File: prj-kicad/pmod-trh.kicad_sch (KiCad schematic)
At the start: 14 parts, among them P1 PMOD, U1 ATSAMD09C13A, U2 SI7021

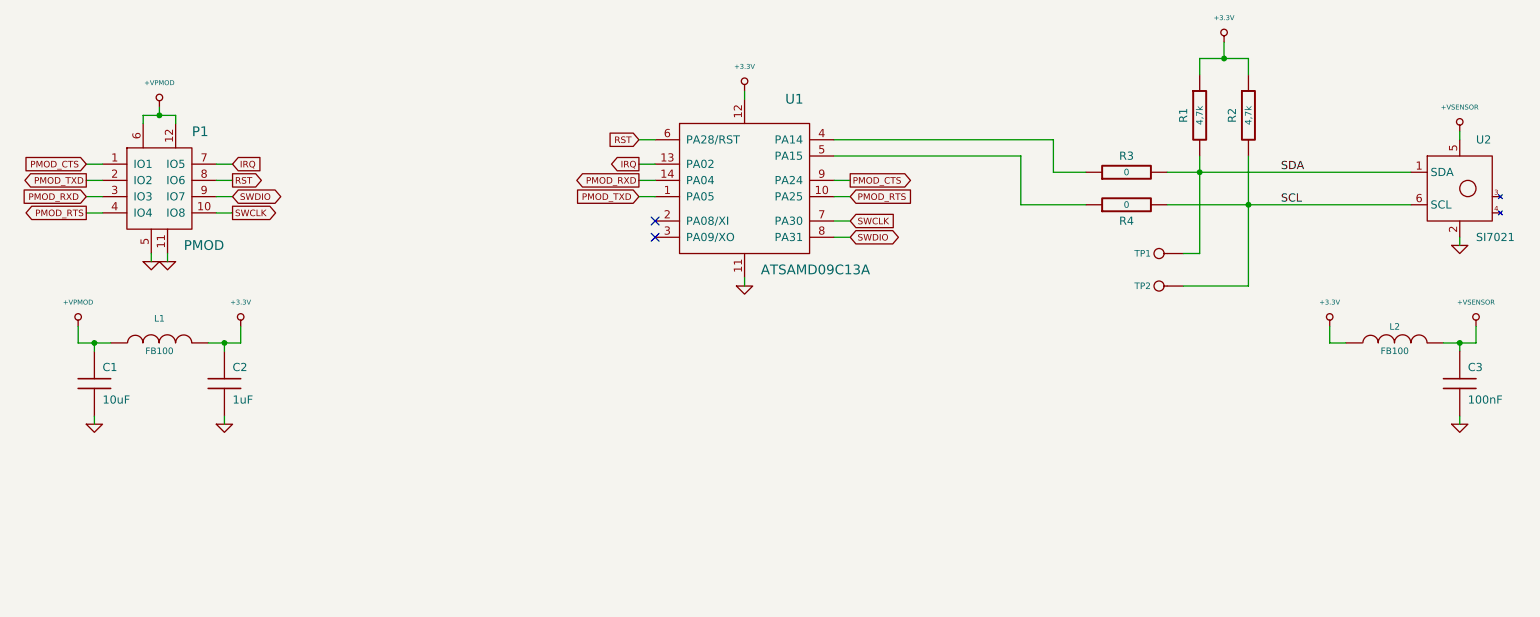
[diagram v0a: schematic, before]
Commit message: Hardware: Create rev2, fix known problems of rev1 (UART, reset) and add power control
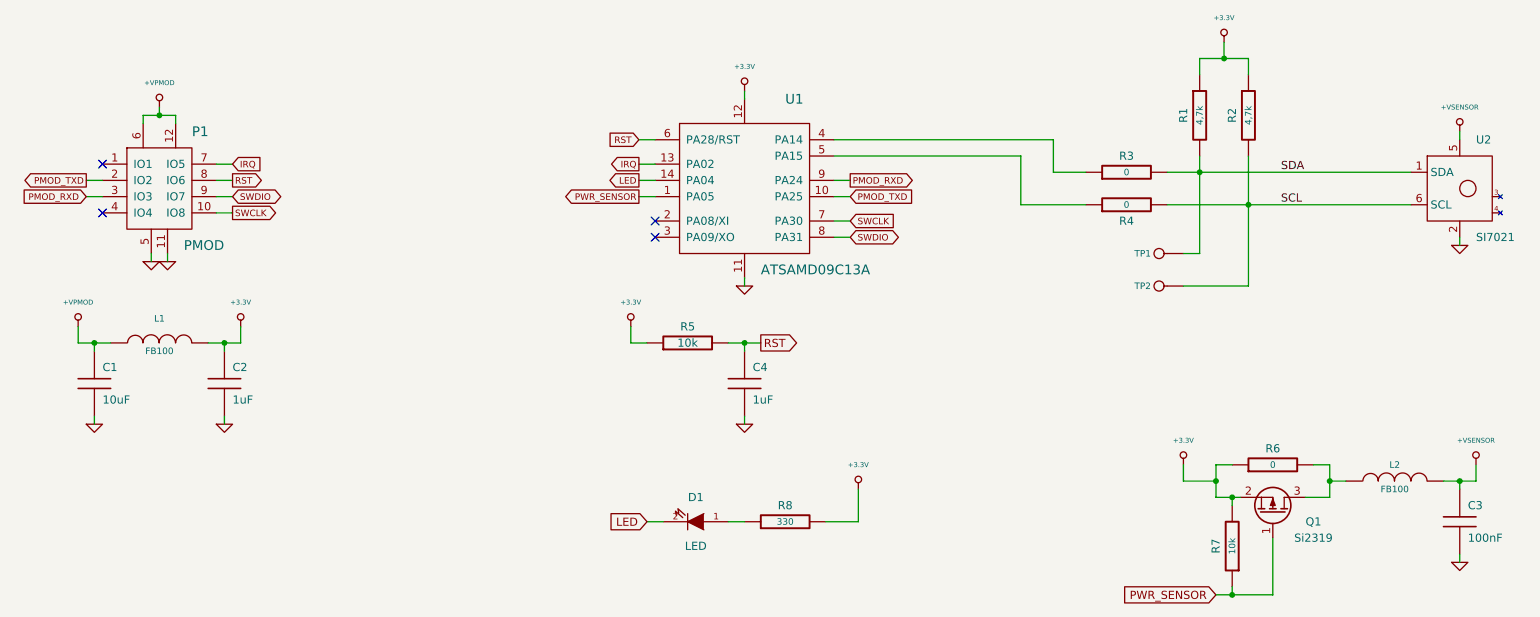
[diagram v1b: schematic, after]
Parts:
- added C4: 1uF, pmod-trh:SMD0603, symbol pmod-trh:C
- added D1: LED, pmod-trh:SMD0805, symbol pmod-trh:LED
- added Q1: Si2319, pmod-trh:SOT23-3, symbol pmod-trh:Q_PMOS
- added R5, R7: 10k, pmod-trh:SMD0603, symbol pmod-trh:R
- added R6: 0, pmod-trh:SMD0603, symbol pmod-trh:R
- added R8: 330, pmod-trh:SMD0603, symbol pmod-trh:R
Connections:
- net +3.3V: now also Q1.2 (S), R5.1, R6.1, R7.2, R8.2; no longer L2.1
- net GND: now also C4.2
- net PMOD_RXD: now also U1.9 (PA24); no longer U1.14 (PA04)
- net PMOD_TXD: now also U1.10 (PA25); no longer U1.1 (PA05)
- net RST: now also C4.1, R5.2
- net PMOD_CTS: no longer names the net of P1.1 (IO1)
- net PMOD_CTS: no longer U1.9 (PA24)
- net PMOD_RTS: no longer names the net of P1.4 (IO4)
- net PMOD_RTS: no longer U1.10 (PA25)
- new net: L2.1, Q1.3 (D), R6.2
- new net: D1.1 (A), R8.1
- new net LED: D1.2 (K), U1.14 (PA04)
- new net PWR_SENSOR: Q1.1 (G), R7.1, U1.1 (PA05)
- no-connect marks 2 -> 4
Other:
- moved on the sheet: C3, L2
